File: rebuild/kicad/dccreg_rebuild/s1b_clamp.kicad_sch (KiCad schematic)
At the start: 13 parts

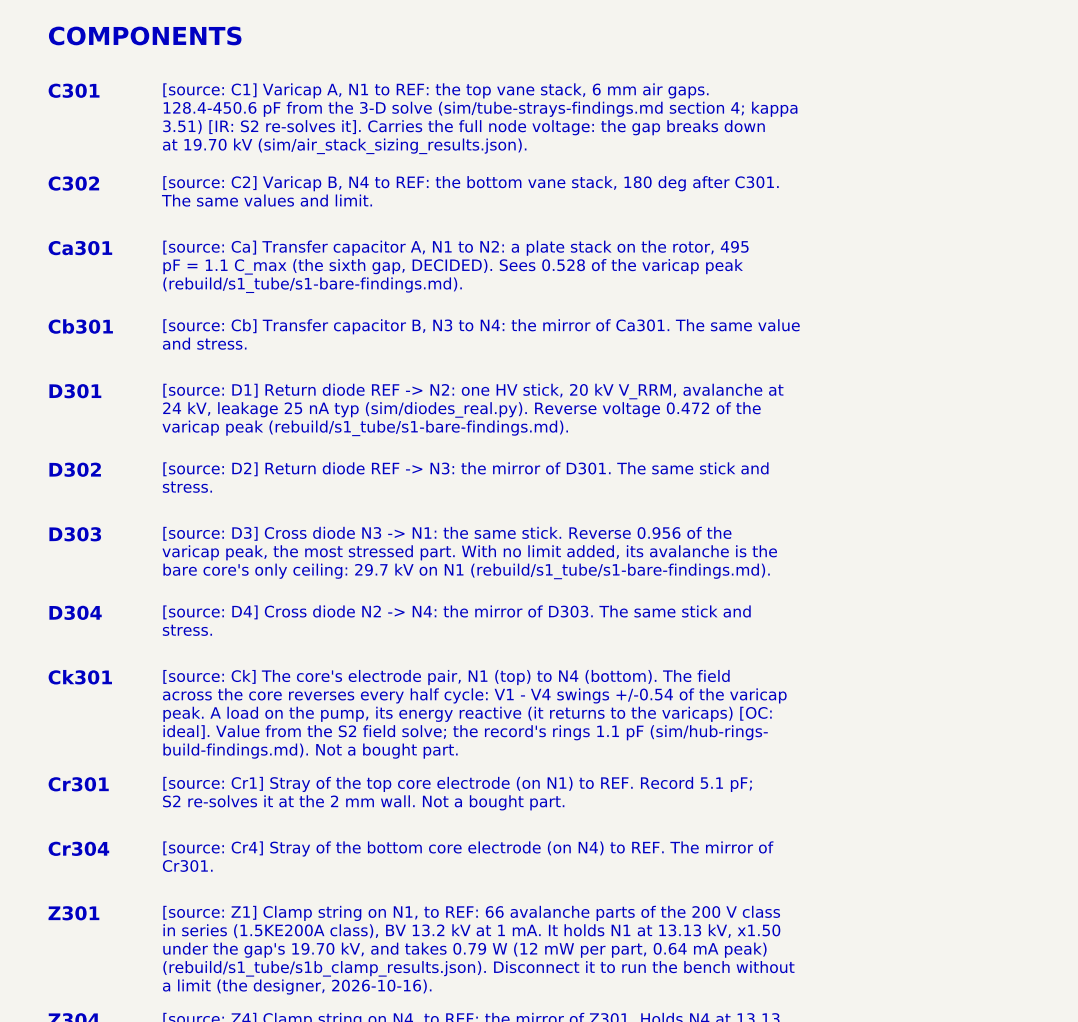
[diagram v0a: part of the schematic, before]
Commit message: feat(rebuild): S2 begins, the plan and the compact deck
The designer's starting choices for S2 (the 3-D models): the 10-11
redesign layout stripped back to the S1b circuit, N1 on side A below the
hub as the record, a rim variant to win back kappa, and the repo's
finite-volume field solver. FreeCAD 1.1.4 is installed beside KiCad.
rebuild/s2_models/s2-plan.md sets out S2a-S2d.

rebuild/s2_models/s2_deck.py plans the deck for the S1b parts only (the
designer: "a bigger deck then required would insert an unnecessary
compromise"), on the redesign study's rules:
- every HV part also clears the grounded can in air (the designer's
  choice): deck r 50-125 against the redesign's r 50-150;
- each clamp string split into two series halves placed against the
  sticks, so the deck balances to 9 g, where a chain plan needed 388 g;
- the column 13 mm off the deck instead of 39, so each side is 26 mm
  shorter;
- the cross wires run straight across, held at the midplane by a PTFE
  bracket with two ribs (41.9 mm creepage against 31.6 needed), as the
  designer asked for now.

Also corrected: N1 is side A (below the hub) in the S1 texts, the S1b
study (re-run, results unchanged) and the KiCad legends (regenerated;
netlists still match, ERC 0/0).

Co-Authored-By: Claude Opus 5.5 <noreply@anthropic.com>
Claude-Session: https://claude.ai/code/session_01EZwGpTFL1hyaEya41kJtBw
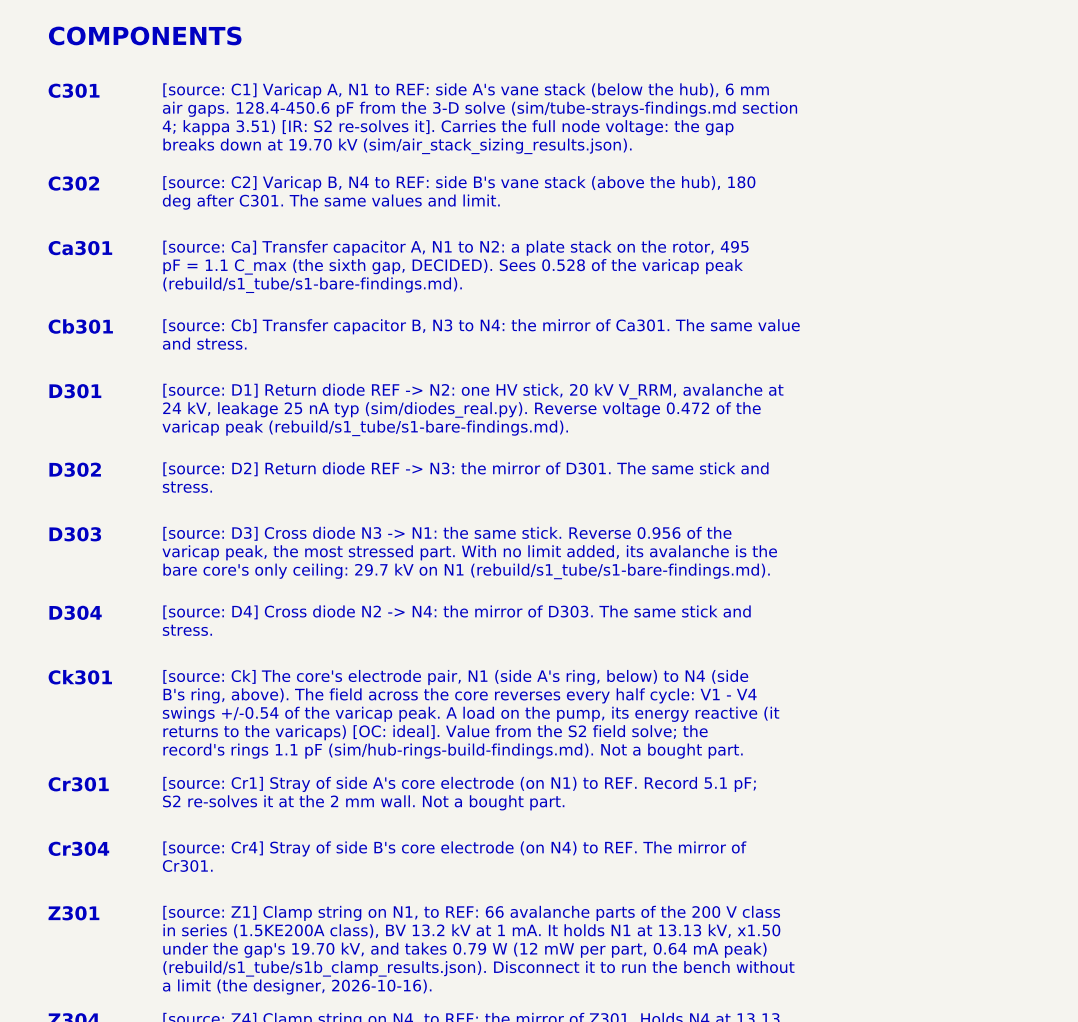
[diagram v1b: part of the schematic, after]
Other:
- note added: "[source: C1] Varicap A, N1 to REF: side A's vane stack (below the hub), 6 mm air gaps. 128.4-450.6 pF from the 3-D solve (sim/tube-strays-findings.md section 4; kappa 3.51) [IR: S2 re-solves it]. Carries the full node voltage: the gap breaks down at 19.70 kV (sim/air_stack_sizing_results.json)."
- note added: "[source: C2] Varicap B, N4 to REF: side B's vane stack (above the hub), 180 deg after C301. The same values and limit."
- note added: "[source: Ck] The core's electrode pair, N1 (side A's ring, below) to N4 (side B's ring, above). The field across the core reverses every half cycle: V1 - V4 swings +/-0.54 of the varicap peak. A load on the pump, its energy reactive (it returns to the varicaps) [OC: ideal]. Value from the S2 field solve; the record's rings 1.1 pF (sim/hub-rings-build-findings.md). Not a bought part."
- note added: "[source: Cr1] Stray of side A's core electrode (on N1) to REF. Record 5.1 pF; S2 re-solves it at the 2 mm wall. Not a bought part."
- note added: "[source: Cr4] Stray of side B's core electrode (on N4) to REF. The mirror of Cr301."
- note removed: "[source: C1] Varicap A, N1 to REF: the top vane stack, 6 mm air gaps. 128.4-450.6 pF from the 3-D solve (sim/tube-strays-findings.md section 4; kappa 3.51) [IR: S2 re-solves it]. Carries the full node voltage: the gap breaks down at 19.70 kV (sim/air_stack_sizing_results.json)."
- note removed: "[source: C2] Varicap B, N4 to REF: the bottom vane stack, 180 deg after C301. The same values and limit."
- note removed: "[source: Ck] The core's electrode pair, N1 (top) to N4 (bottom). The field across the core reverses every half cycle: V1 - V4 swings +/-0.54 of the varicap peak. A load on the pump, its energy reactive (it returns to the varicaps) [OC: ideal]. Value from the S2 field solve; the record's rings 1.1 pF (sim/hub-rings- build-findings.md). Not a bought part."
- note removed: "[source: Cr1] Stray of the top core electrode (on N1) to REF. Record 5.1 pF; S2 re-solves it at the 2 mm wall. Not a bought part."
- note removed: "[source: Cr4] Stray of the bottom core electrode (on N4) to REF. The mirror of Cr301."
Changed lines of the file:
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@@
 		)
 	)
-	(text "[source: C1] Varicap A, N1 to REF: the top vane stack, 6 mm air gaps.\n128.4-450.6 pF from the 3-D solve (sim/tube-strays-findings.md section 4; kappa\n3.51) [IR: S2 re-solves it]. Carries the full node voltage: the gap breaks down\nat 19.70 kV (sim/air_stack_sizing_results.json)."
+	(text "[source: C1] Varicap A, N1 to REF: side A's vane stack (below the hub), 6 mm\nair gaps. 128.4-450.6 pF from the 3-D solve (sim/tube-strays-findings.md section\n4; kappa 3.51) [IR: S2 re-solves it]. Carries the full node voltage: the gap\nbreaks down at 19.70 kV (sim/air_stack_sizing_results.json)."
 		(exclude_from_sim yes)
 		(at 307.34 21.59 0)
@@
 		)
 	)
-	(text "[source: C2] Varicap B, N4 to REF: the bottom vane stack, 180 deg after C301.\nThe same values and limit."
+	(text "[source: C2] Varicap B, N4 to REF: side B's vane stack (above the hub), 180\ndeg after C301. The same values and limit."
 		(exclude_from_sim yes)
 		(at 307.34 31.90 0)
@@
 		)
 	)
-	(text "[source: Ck] The core's electrode pair, N1 (top) to N4 (bottom). The field\nacross the core reverses every half cycle: V1 - V4 swings +/-0.54 of the varicap\npeak. A load on the pump, its energy reactive (it returns to the varicaps) [OC:\nideal]. Value from the S2 field solve; the record's rings 1.1 pF (sim/hub-rings-\nbuild-findings.md). Not a bought part."
+	(text "[source: Ck] The core's electrode pair, N1 (side A's ring, below) to N4 (side\nB's ring, above). The field across the core reverses every half cycle: V1 - V4\nswings +/-0.54 of the varicap peak. A load on the pump, its energy reactive (it\nreturns to the varicaps) [OC: ideal]. Value from the S2 field solve; the\nrecord's rings 1.1 pF (sim/hub-rings-build-findings.md). Not a bought part."
 		(exclude_from_sim yes)
 		(at 307.34 86.77 0)
@@
 		)
 	)
-	(text "[source: Cr1] Stray of the top core electrode (on N1) to REF. Record 5.1 pF;\nS2 re-solves it at the 2 mm wall. Not a bought part."
+	(text "[source: Cr1] Stray of side A's core electrode (on N1) to REF. Record 5.1 pF;\nS2 re-solves it at the 2 mm wall. Not a bought part."
 		(exclude_from_sim yes)
 		(at 307.34 98.65 0)
@@
 		)
 	)
-	(text "[source: Cr4] Stray of the bottom core electrode (on N4) to REF. The mirror of\nCr301."
+	(text "[source: Cr4] Stray of side B's core electrode (on N4) to REF. The mirror of\nCr301."
 		(exclude_from_sim yes)
 		(at 307.34 105.82 0)
@@
 			)
 		)
-		(property "Description" "Varicap A, N1 to REF: the top vane stack, 6 mm air gaps. 128.4-450.6 pF from the 3-D solve (sim/tube-strays-findings.md section 4; kappa 3.51) [IR: S2 re-solves it]. Carries the full node voltage: the gap breaks down at 19.70 kV (sim/air_stack_sizing_results.json)."
+		(property "Description" "Varicap A, N1 to REF: side A's vane stack (below the hub), 6 mm air gaps. 128.4-450.6 pF from the 3-D solve (sim/tube-strays-findings.md section 4; kappa 3.51) [IR: S2 re-solves it]. Carries the full node voltage: the gap breaks down at 19.70 kV (sim/air_stack_sizing_results.json)."
 			(at 71.12 167.64 0)
 			(hide yes)
@@
 			)
 		)
-		(property "Description" "Varicap B, N4 to REF: the bottom vane stack, 180 deg after C301. The same values and limit."
+		(property "Description" "Varicap B, N4 to REF: side B's vane stack (above the hub), 180 deg after C301. The same values and limit."
 			(at 223.52 167.64 0)
 			(hide yes)
@@
 			)
 		)
-		(property "Description" "The core's electrode pair, N1 (top) to N4 (bottom). The field across the core reverses every half cycle: V1 - V4 swings +/-0.54 of the varicap peak. A load on the pump, its energy reactive (it returns to the varicaps) [OC: ideal]. Value from the S2 field solve; the record's rings 1.1 pF (sim/hub-rings-build-findings.md). Not a bought part."
+		(property "Description" "The core's electrode pair, N1 (side A's ring, below) to N4 (side B's ring, above). The field across the core reverses every half cycle: V1 - V4 swings +/-0.54 of the varicap peak. A load on the pump, its energy reactive (it returns to the varicaps) [OC: ideal]. Value from the S2 field solve; the record's rings 1.1 pF (sim/hub-rings-build-findings.md). Not a bought part."
 			(at 147.32 45.72 90)
 			(hide yes)
@@
 			)
 		)
-		(property "Description" "Stray of the top core electrode (on N1) to REF. Record 5.1 pF; S2 re-solves it at the 2 mm wall. Not a bought part."
+		(property "Description" "Stray of side A's core electrode (on N1) to REF. Record 5.1 pF; S2 re-solves it at the 2 mm wall. Not a bought part."
 			(at 33.02 167.64 0)
 			(hide yes)
@@
 			)
 		)
-		(property "Description" "Stray of the bottom core electrode (on N4) to REF. The mirror of Cr301."
+		(property "Description" "Stray of side B's core electrode (on N4) to REF. The mirror of Cr301."
 			(at 261.62 167.64 0)
 			(hide yes)
